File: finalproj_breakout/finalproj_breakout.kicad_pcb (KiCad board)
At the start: 2 copper layers, 76.5 x 65 mm, 29 parts, among them J1 Conn_02x18_Odd_Even, J2 Conn_02x18_Odd_Even, J3 Conn_02x18_Odd_Even, J4 Conn_02x18_Odd_Even, J8 Programmer_Conn, SW1 RESET_SW, U1 STM32F767ZITx

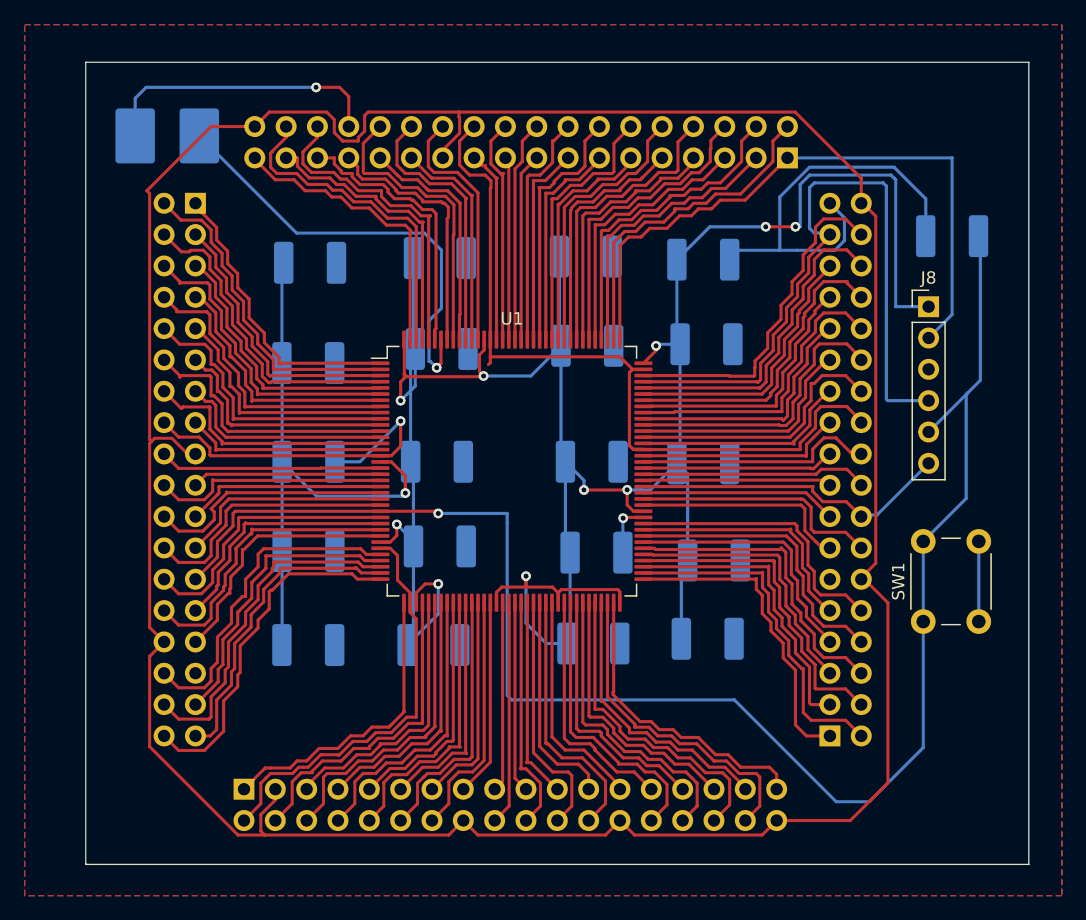
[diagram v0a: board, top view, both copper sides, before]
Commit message: Removed unused files (breakoutalt), fixed alignment issue of header pins
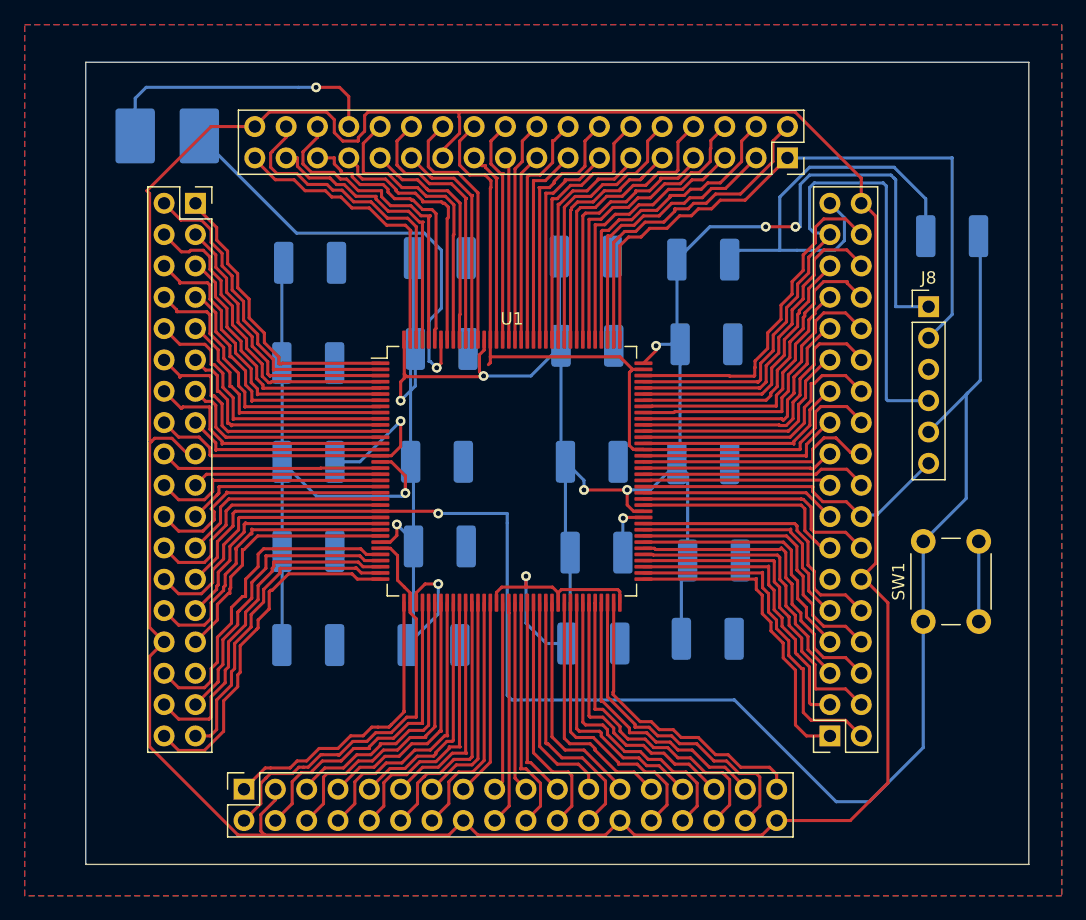
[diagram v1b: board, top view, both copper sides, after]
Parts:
- J1, J2, J3, J4: footprint Connector_PinHeader_2.54mm:PinHeader_2x18_P2.54mm_Vertical -> Connector_PinHeader_2.54mm:PinHeader_2x18_P2.54mm_Vertical_DoubleSided

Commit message: fixed DRC erros on main board, had to revert breakout board headers to one sided since couldn't find lib
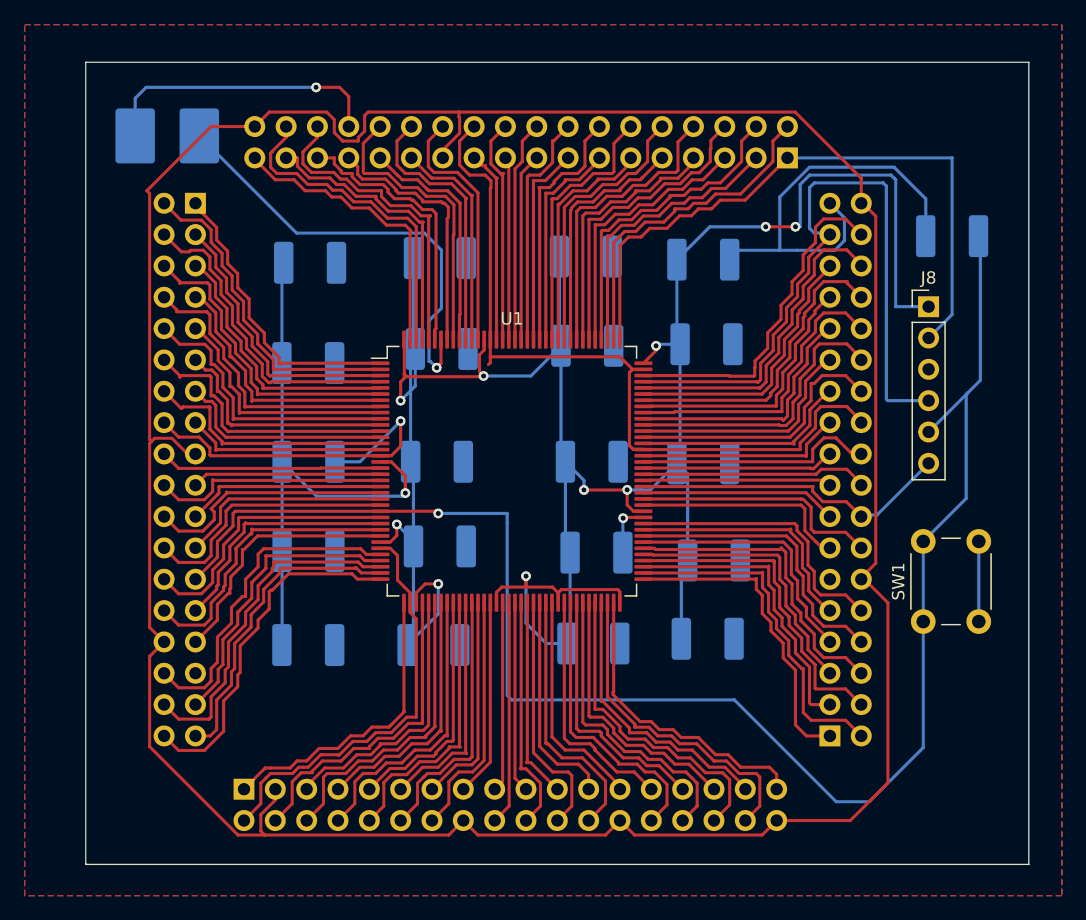
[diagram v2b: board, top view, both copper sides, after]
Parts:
- J1, J2, J3, J4: footprint Connector_PinHeader_2.54mm:PinHeader_2x18_P2.54mm_Vertical_DoubleSided -> Connector_PinHeader_2.54mm:PinHeader_2x18_P2.54mm_Vertical
